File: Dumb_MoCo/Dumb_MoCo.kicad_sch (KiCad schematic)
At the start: 17 parts

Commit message: Started new VNH layout
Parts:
- removed Conn3: Molex_SL_07, MRDT_Connectors:MOLEX_SL_07_Horizontal, symbol MRDT_Connectors:Molex_SL_07
- removed R4: 1k, Resistor_SMD:R_0603_1608Metric_Pad0.98x0.95mm_HandSolder, symbol Device:R
- removed U2: ~, Package_SO:ST_PowerSSO-36_TP, symbol MRDT_Devices:VNH5050A-E
- removed V1, V2, V3, V4: Via, MRDT_Drill_Holes:4_40_Hole, symbol MRDT_Drill_Holes:Via
- added Conn3: Molex_SL_05, MRDT_Connectors:MOLEX_SL_05_Horizontal, symbol MRDT_Connectors:Molex_SL_05
- added H1, H2, H3, H4: MountingHole, MRDT_Drill_Holes:4_40_Hole, symbol Mechanical:MountingHole
- added R6: 3.3k, Resistor_SMD:R_0603_1608Metric_Pad0.98x0.95mm_HandSolder, symbol Device:R
- added U1: VNH5050A-E, Package_SO:ST_PowerSSO-36_TP, symbol MRDT_Devices:VNH5050A-E
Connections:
- net +12V: now also U1.13 (VCC), U1.24 (VCC)
- net CS: now also Conn3.3
- net GND: now also U1.1 (GND_A), U1.20 (CS_DIS), U1.3 (GND_A), U1.30 (GND_B), U1.31 (GND_B), U1.32 (GND_B), U1.33 (GND_B), U1.34 (GND_B), U1.36 (GND_B), U1.4 (GND_A), U1.5 (GND_A), U1.6 (GND_A), U1.7 (GND_A)
- net IN_A: now also Conn3.4
- net IN_B: now also Conn3.1
- net PWM: now also Conn3.2
- net at R1.1, R2.1: now also U1.19 (CS)
- net at R5.2: now also U1.15 (INA)
- net at Conn1.2 (V+Log): now also U1.23 (OUT_B), U1.25 (OUT_B), U1.26 (OUT_B), U1.27 (OUT_B), U1.28 (OUT_B), U1.29 (OUT_B), U1.35 (OUT_B)
- net at R3.2: now also U1.17 (PWM)
- net at R7.2: now also U1.16 (DIAG_A/EN_A)
- net at Conn1.1 (GND): now also U1.10 (OUT_A), U1.11 (OUT_A), U1.12 (OUT_A), U1.14 (OUT_A), U1.2 (OUT_A), U1.8 (OUT_A), U1.9 (OUT_A)
- net at R6.2: now also U1.22 (INB)
- net +5V renamed +3V3
- net +3V3: now also Conn3.5, R6.1
- new net: R6.2, U1.21 (DIAG_B/EN_B)

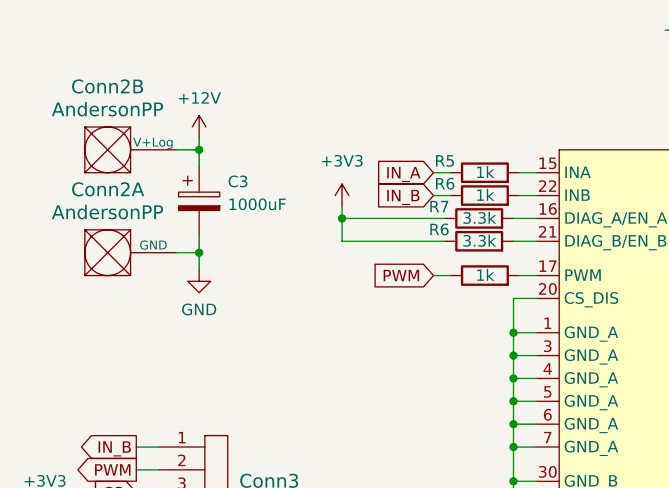
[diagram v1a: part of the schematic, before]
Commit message: Added vias and changed bulk cap
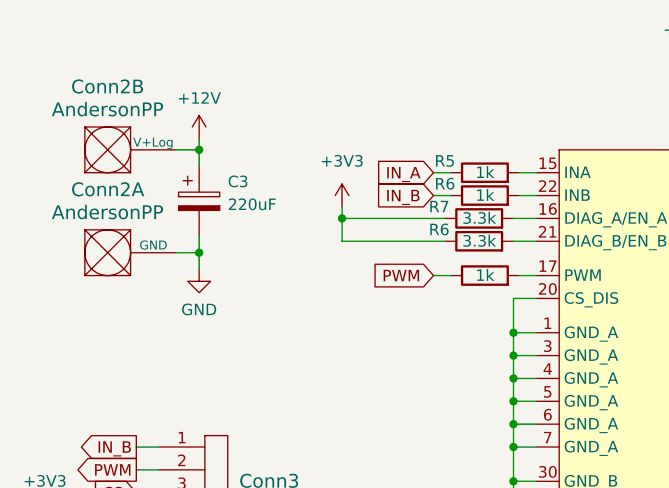
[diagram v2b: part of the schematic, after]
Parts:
- C3: value 1000uF -> 220uF; footprint Capacitor_THT:CP_Radial_D10.0mm_P5.00mm -> Capacitor_THT:C_Radial_D6.3mm_H11.0mm_P2.50mm
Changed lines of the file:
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@@
 			)
 		)
-		(property "Value" "1000uF"
+		(property "Value" "220uF"
 			(at 43.18 37.846 0)
 			(effects
@@
 			)
 		)
-		(property "Footprint" "Capacitor_THT:CP_Radial_D10.0mm_P5.00mm"
+		(property "Footprint" "Capacitor_THT:C_Radial_D6.3mm_H11.0mm_P2.50mm"
 			(at 40.9702 41.275 0)
 			(effects

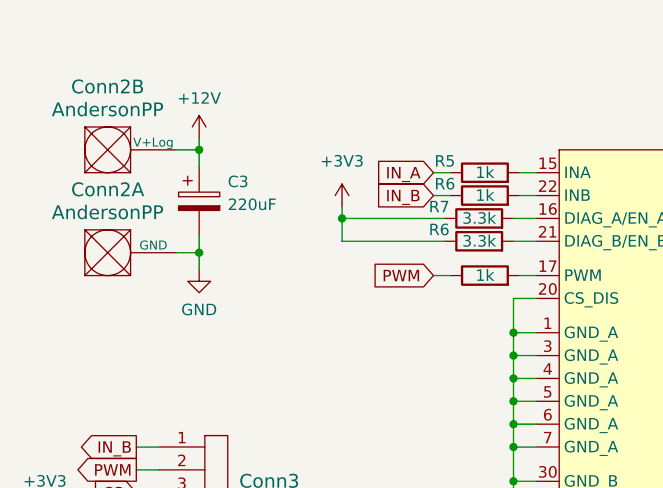
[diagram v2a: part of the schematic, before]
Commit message: Changed Bulk cap to 330uF
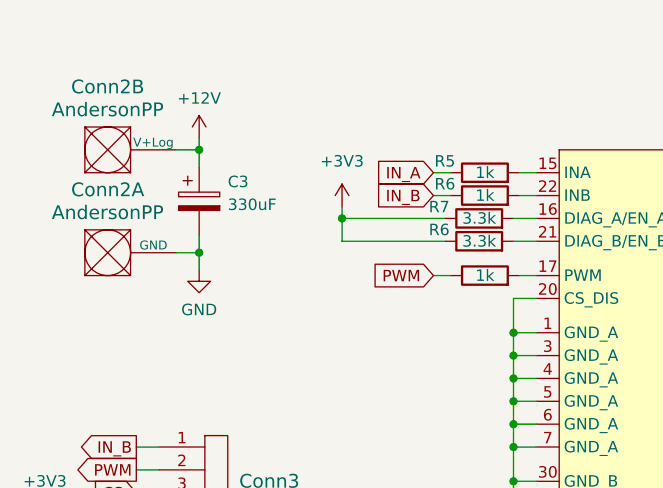
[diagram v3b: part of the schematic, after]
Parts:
- C3: value 220uF -> 330uF; footprint Capacitor_THT:C_Radial_D6.3mm_H11.0mm_P2.50mm -> Capacitor_THT:C_Radial_D8.0mm_H11.5mm_P3.50mm
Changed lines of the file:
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@@
 			)
 		)
-		(property "Value" "220uF"
+		(property "Value" "330uF"
 			(at 43.18 37.846 0)
 			(effects
@@
 			)
 		)
-		(property "Footprint" "Capacitor_THT:C_Radial_D6.3mm_H11.0mm_P2.50mm"
+		(property "Footprint" "Capacitor_THT:C_Radial_D8.0mm_H11.5mm_P3.50mm"
 			(at 40.9702 41.275 0)
 			(effects
